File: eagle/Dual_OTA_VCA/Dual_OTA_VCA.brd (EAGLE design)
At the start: 100 x 80 mm, 61 parts, among them IC1 LM13600N, IC2 NJM4580, IC3 LM4558N, IC4 NJM4580, T1 2SA1015, T2 2SA1015

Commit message: before Parts layout
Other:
- board size 100 x 80 mm -> 93.7 x 71.1 mm
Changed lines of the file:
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@@
 <layer number="97" name="Info" color="7" fill="1" visible="no" active="no"/>
 <layer number="98" name="Guide" color="6" fill="1" visible="no" active="no"/>
+<layer number="100" name="Gude" color="11" fill="1" visible="yes" active="yes"/>
 </layers>
 <board>
 <plain>
-<wire x1="0" y1="0" x2="100" y2="0" width="0" layer="20"/>
-<wire x1="100" y1="0" x2="100" y2="80" width="0" layer="20"/>
-<wire x1="100" y1="80" x2="0" y2="80" width="0" layer="20"/>
-<wire x1="0" y1="80" x2="0" y2="0" width="0" layer="20"/>
+<wire x1="0" y1="0" x2="93.65" y2="0" width="0" layer="20"/>
+<wire x1="93.65" y1="0" x2="93.65" y2="71.11" width="0" layer="20"/>
+<wire x1="93.65" y1="71.11" x2="0" y2="71.11" width="0" layer="20"/>
+<wire x1="0" y1="71.11" x2="0" y2="0" width="0" layer="20"/>
+<wire x1="2.54" y1="2.54" x2="2.54" y2="12.7" width="0" layer="100"/>
+<wire x1="2.54" y1="12.7" x2="2.54" y2="25.4" width="0" layer="100"/>
+<wire x1="2.54" y1="25.4" x2="2.54" y2="38.1" width="0" layer="100"/>
+<wire x1="2.54" y1="38.1" x2="2.54" y2="50.8" width="0" layer="100"/>
+<wire x1="2.54" y1="50.8" x2="2.54" y2="63.5" width="0" layer="100"/>
+<wire x1="2.54" y1="63.5" x2="2.54" y2="68.58" width="0" layer="100"/>
+<wire x1="2.54" y1="2.54" x2="12.7" y2="2.54" width="0" layer="100"/>
+<wire x1="12.7" y1="2.54" x2="25.4" y2="2.54" width="0" layer="100"/>
+<wire x1="25.4" y1="2.54" x2="38.1" y2="2.54" width="0" layer="100"/>
+<wire x1="38.1" y1="2.54" x2="50.8" y2="2.54" width="0" layer="100"/>
+<wire x1="50.8" y1="2.54" x2="63.5" y2="2.54" width="0" layer="100"/>
+<wire x1="63.5" y1="2.54" x2="76.2" y2="2.54" width="0" layer="100"/>
+<wire x1="76.2" y1="2.54" x2="88.9" y2="2.54" width="0" layer="100"/>
+<wire x1="88.9" y1="2.54" x2="91.44" y2="2.54" width="0" layer="100"/>
+<wire x1="12.7" y1="2.54" x2="12.7" y2="68.58" width="0" layer="100"/>
+<wire x1="25.4" y1="2.54" x2="25.4" y2="68.58" width="0" layer="100"/>
+<wire x1="38.1" y1="2.54" x2="38.1" y2="68.58" width="0" layer="100"/>
+<wire x1="50.8" y1="2.54" x2="50.8" y2="68.58" width="0" layer="100"/>
+<wire x1="63.5" y1="2.54" x2="63.5" y2="68.58" width="0" layer="100"/>
+<wire x1="76.2" y1="2.54" x2="76.2" y2="68.58" width="0" layer="100"/>
+<wire x1="88.9" y1="2.54" x2="88.9" y2="68.58" width="0" layer="100"/>
+<wire x1="2.54" y1="12.7" x2="91.44" y2="12.7" width="0" layer="100"/>
+<wire x1="2.54" y1="25.4" x2="91.44" y2="25.4" width="0" layer="100"/>
+<wire x1="2.54" y1="38.1" x2="91.44" y2="38.1" width="0" layer="100"/>
+<wire x1="2.54" y1="50.8" x2="91.44" y2="50.8" width="0" layer="100"/>
+<wire x1="2.54" y1="63.5" x2="91.44" y2="63.5" width="0" layer="100"/>
+<wire x1="2.54" y1="68.58" x2="91.44" y2="68.58" width="0" layer="100"/>
+<wire x1="91.44" y1="68.58" x2="91.44" y2="2.54" width="0" layer="100"/>
+<hole x="2.54" y="68.58" drill="3.2"/>
+<hole x="2.54" y="2.54" drill="3.2"/>
+<hole x="91.44" y="2.54" drill="3.2"/>
+<hole x="91.44" y="68.58" drill="3.2"/>
 </plain>
 <attributes>

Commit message: Update the eagle files
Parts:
- C6, C7: device rcl:C025-024X044 -> rcl:C050-024X044
- moved JP9 63.8 mm to (22.9, 11.4), turned to 270 degrees
- moved C5 41.1 mm to (7.62, 24.1), turned to 90 degrees
- moved JP10 20.5 mm to (40.6, 20.3)
- moved C7 18.3 mm to (73.7, 27.9)
- moved JP17 18.0 mm to (43.2, 50.8)
- moved C4 17.8 mm to (7.62, 47.0), turned to 90 degrees
- moved JP14 16.1 mm to (74.9, 58.4)
- moved R10 15.7 mm to (21.6, 58.4)
- moved JP8 15.5 mm to (8.89, 55.9)
- moved C6 15.3 mm to (73.7, 40.6), turned to 180 degrees
- moved JP7 15.3 mm to (8.89, 58.4)
- moved R1 14.9 mm to (67.3, 17.8), turned to 180 degrees
- moved C15 14.5 mm to (86.4, 41.9), turned to 270 degrees
- moved JP11 13.3 mm to (74.9, 55.9)
- moved T1 13.1 mm to (58.4, 22.9)
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
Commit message: Board Design
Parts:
- R1, R11: value 82k -> 56k
- moved JP15 9.67 mm to (10.2, 49.5), turned to 90 degrees
- moved C4 8.03 mm to (10.2, 39.4)
- moved C10 8.03 mm to (15.2, 41.9)
- moved JP5 7.41 mm to (7.62, 19.1), turned to 270 degrees
- moved JP16 6.48 mm to (88.9, 54.6), turned to 90 degrees
- moved JP13 6.48 mm to (12.7, 49.5), turned to 90 degrees
- moved C5 5.68 mm to (10.2, 29.2)
- moved JP7 5.68 mm to (11.4, 63.5)
- moved JP9 5.08 mm to (22.9, 16.5)
- moved R20 5.08 mm to (35.6, 48.3)
- moved IC3 5.08 mm to (19.1, 34.3)
- moved R7 5.08 mm to (20.3, 25.4)
- moved C11 5.08 mm to (25.4, 29.2)
- moved LED1 5.08 mm to (21.6, 63.5)
- moved R18 5.08 mm to (22.9, 43.2), turned to 180 degrees
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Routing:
- net AGND: track 0.00 -> 473.2 mm, vias 0 -> 3
- net -5V: track 0.00 -> 253.1 mm, vias 0 -> 4
- net +5V: track 0.00 -> 145.8 mm
- net N$18: track 0.00 -> 30.0 mm
- net N$12: track 0.00 -> 27.9 mm
- net N$32: track 0.00 -> 26.5 mm
- net N$7: track 0.00 -> 25.4 mm, vias 0 -> 2
- net N$34: track 0.00 -> 25.4 mm, vias 0 -> 2
- net N$5: track 0.00 -> 17.8 mm, vias 0 -> 2
- net N$8: track 0.00 -> 15.2 mm
- net N$28: track 0.00 -> 15.2 mm, vias 0 -> 1
- net N$25: track 0.00 -> 15.2 mm, vias 0 -> 2
- net N$3: track 0.00 -> 15.2 mm
- net N$23: track 0.00 -> 15.2 mm
- net N$10: track 0.00 -> 13.8 mm
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
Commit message: Update Board Design
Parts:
- moved JP5 2.54 mm to (10.2, 19.1)
- moved JP10 2.54 mm to (43.2, 17.8)
- moved JP2 2.54 mm to (12.7, 19.1)
- moved LED1 2.54 mm to (24.1, 63.5)
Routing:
- net AGND: track 473.2 -> 484.9 mm, vias 3 -> 4
- net N$15: track 0.00 -> 7.62 mm
- net N$28: track 15.2 -> 20.3 mm, vias 1 -> 2
- net -5V: track 253.1 -> 257.2 mm
- net N$32: track 26.5 -> 30.0 mm, vias 0 -> 2
- net +5V: track 145.8 -> 148.4 mm
- net N$25: track 15.2 -> 17.8 mm
- net N$18: track 30.0 -> 32.6 mm, vias 0 -> 2
- net N$7: track 25.4 -> 27.9 mm
- net N$26: track 11.2 -> 13.8 mm
- net N$10: track 13.8 -> 15.2 mm

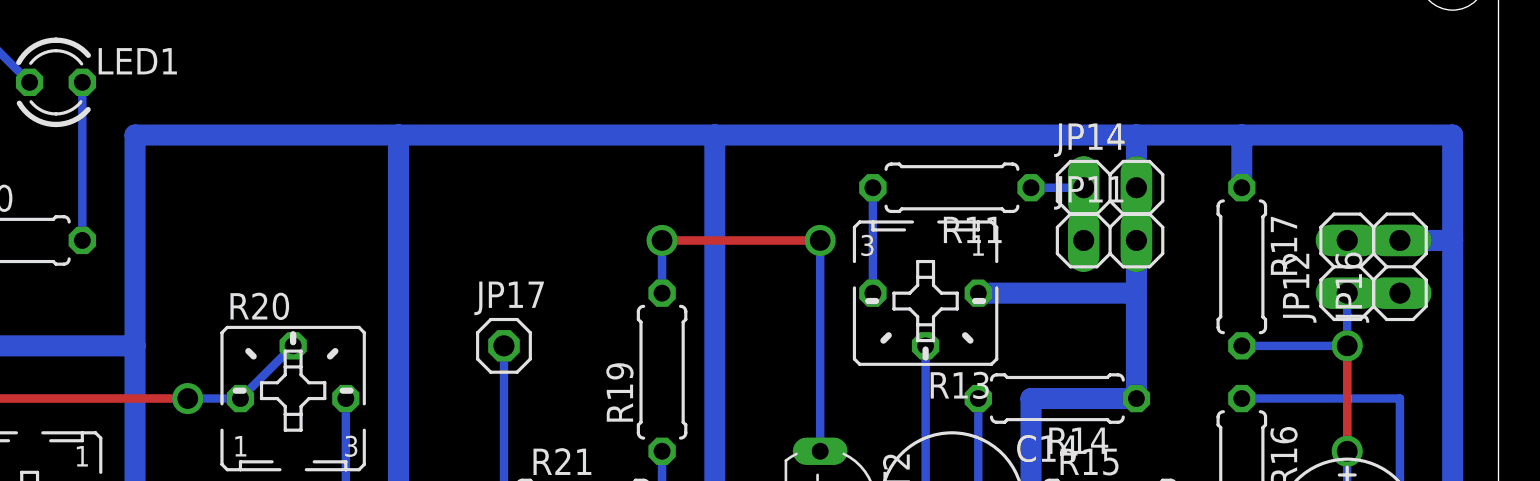
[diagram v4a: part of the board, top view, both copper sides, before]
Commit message: Update Board Design. Add テスト表
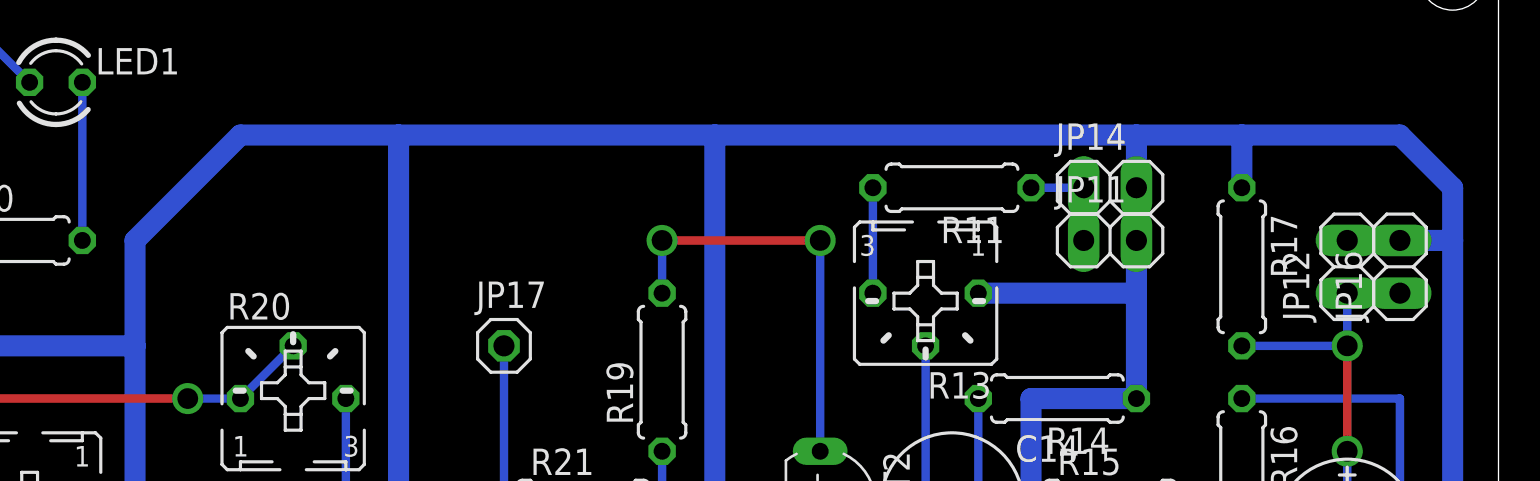
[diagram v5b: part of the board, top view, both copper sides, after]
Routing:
- net AGND: track 484.9 -> 480.4 mm
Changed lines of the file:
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@@
 <wire x1="55.88" y1="60.96" x2="76.2" y2="60.96" width="1.016" layer="16"/>
 <wire x1="76.2" y1="60.96" x2="81.28" y2="60.96" width="1.016" layer="16"/>
-<wire x1="81.28" y1="60.96" x2="91.44" y2="60.96" width="1.016" layer="16"/>
-<wire x1="91.44" y1="60.96" x2="91.44" y2="55.88" width="1.016" layer="16"/>
 <wire x1="81.28" y1="58.42" x2="81.28" y2="60.96" width="1.016" layer="16"/>
 <wire x1="76.2" y1="58.42" x2="76.2" y2="60.96" width="1.016" layer="16"/>
@@
 <wire x1="27.94" y1="40.64" x2="27.94" y2="43.18" width="1.016" layer="16"/>
 <wire x1="27.94" y1="43.18" x2="27.94" y2="50.8" width="1.016" layer="16"/>
-<wire x1="27.94" y1="50.8" x2="27.94" y2="60.96" width="1.016" layer="16"/>
-<wire x1="27.94" y1="60.96" x2="40.64" y2="60.96" width="1.016" layer="16"/>
 <wire x1="25.4" y1="43.18" x2="27.94" y2="43.18" width="1.016" layer="16"/>
 <wire x1="10.16" y1="40.64" x2="7.62" y2="40.64" width="1.016" layer="16"/>
@@
 <via x="40.64" y="15.24" extent="1-16" drill="1" shape="square"/>
 <via x="25.4" y="15.24" extent="1-16" drill="1" shape="square"/>
+<wire x1="27.94" y1="50.8" x2="27.94" y2="55.88" width="1.016" layer="16"/>
+<wire x1="27.94" y1="55.88" x2="33.02" y2="60.96" width="1.016" layer="16"/>
+<wire x1="33.02" y1="60.96" x2="40.64" y2="60.96" width="1.016" layer="16"/>
+<wire x1="81.28" y1="60.96" x2="88.9" y2="60.96" width="1.016" layer="16"/>
+<wire x1="88.9" y1="60.96" x2="91.44" y2="58.42" width="1.016" layer="16"/>
+<wire x1="91.44" y1="58.42" x2="91.44" y2="55.88" width="1.016" layer="16"/>
 </signal>
 <signal name="N$1">
